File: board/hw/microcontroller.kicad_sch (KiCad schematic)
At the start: 2 parts, among them U1 RP2040, Y1 Crystal

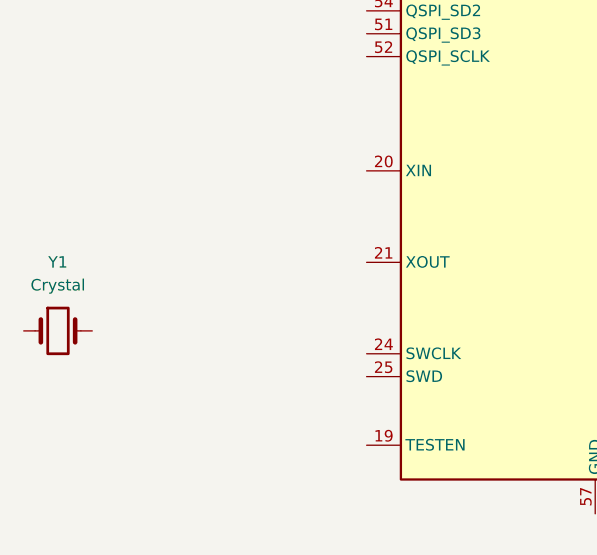
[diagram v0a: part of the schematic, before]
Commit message: added cristal oscillator with capacitors, and 3.3V LDO voltage regulator
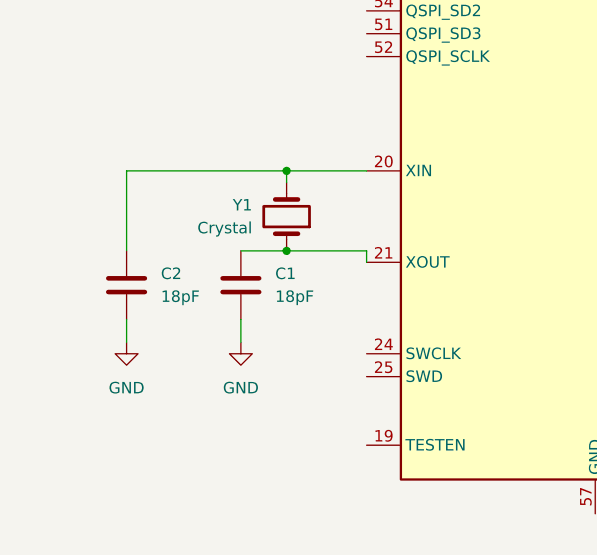
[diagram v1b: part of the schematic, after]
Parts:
- added C1, C2: 18pF, Capacitor_SMD:C_0603_1608Metric, symbol Device:C
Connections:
- net at U1.20 (XIN): now also Y1.2, C2.1
- net at U1.21 (XOUT): now also Y1.1, C1.1
- new net GND: C1.2, C2.2
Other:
- moved on the sheet: Y1
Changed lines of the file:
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@@
 (kicad_sch (version 20230121) (generator eeschema)
   (paper "A4")
+  (junction (at 114.3 101.6) (diameter 0) (color 0 0 0 0)
+  )
+  (junction (at 114.3 110.49) (diameter 0) (color 0 0 0 0)
+  )
+  (wire (pts (xy 96.52 118.11) (xy 96.52 120.65))
+    (stroke (width 0) (type default))
+  )
+  (wire (pts (xy 114.3 101.6) (xy 114.3 102.87))
+    (stroke (width 0) (type default))
+  )
+  (wire (pts (xy 109.22 110.49) (xy 114.3 110.49))
+    (stroke (width 0) (type default))
+  )
+  (wire (pts (xy 123.19 110.49) (xy 123.19 111.76))
+    (stroke (width 0) (type default))
+  )
+  (wire (pts (xy 96.52 101.6) (xy 114.3 101.6))
+    (stroke (width 0) (type default))
+  )
+  (wire (pts (xy 123.19 101.6) (xy 114.3 101.6))
+    (stroke (width 0) (type default))
+  )
+  (wire (pts (xy 109.22 118.11) (xy 109.22 120.65))
+    (stroke (width 0) (type default))
+  )
+  (wire (pts (xy 96.52 110.49) (xy 96.52 101.6))
+    (stroke (width 0) (type default))
+  )
+  (wire (pts (xy 114.3 110.49) (xy 123.19 110.49))
+    (stroke (width 0) (type default))
+  )
   (symbol (lib_id "MCU_RaspberryPi:RP2040") (at 148.59 93.98 0) (unit 1)
     (in_bom yes) (on_board yes) (dnp no) (fields_autoplaced)
@@
     )
   )
-  (symbol (lib_id "Device:Crystal") (at 88.9 119.38 0) (unit 1)
-    (in_bom yes) (on_board yes) (dnp no) (fields_autoplaced)
-    (property "Reference" "Y1" (at 88.9 111.76 0)
+  (symbol (lib_id "Device:Crystal") (at 114.3 106.68 270) (mirror x) (unit 1)
+    (in_bom yes) (on_board yes) (dnp no)
+    (property "Reference" "Y1" (at 110.49 105.41 90)
+      (effects (font (size 1.27 1.27)) (justify right))
+    )
+    (property "Value" "Crystal" (at 110.49 107.95 90)
+      (effects (font (size 1.27 1.27)) (justify right))
+    )
+    (property "Footprint" "Crystal:Crystal_SMD_SeikoEpson_MA505-2Pin_12.7x5.1mm" (at 114.3 106.68 0)
+      (effects (font (size 1.27 1.27)) hide)
+    )
+    (property "Datasheet" "~" (at 114.3 106.68 0)
+      (effects (font (size 1.27 1.27)) hide)
+    )
+    (pin "2")
+    (pin "1")
+    (instances
+      (project "yals"
+        (path "/920838ab-42d6-4f6a-a4ed-bf4606dd42d5/8ac632fc-8d3b-4983-8745-f2671c397aa7"
+          (reference "Y1") (unit 1)
+        )
+      )
+    )
+  )
+  (symbol (lib_id "Device:C") (at 96.52 114.3 0) (unit 1)
+    (in_bom yes) (on_board yes) (dnp no) (fields_autoplaced)
+    (property "Reference" "C2" (at 100.33 113.03 0)
+      (effects (font (size 1.27 1.27)) (justify left))
+    )
+    (property "Value" "18pF" (at 100.33 115.57 0)
+      (effects (font (size 1.27 1.27)) (justify left))
+    )
+    (property "Footprint" "Capacitor_SMD:C_0603_1608Metric" (at 97.4852 118.11 0)
+      (effects (font (size 1.27 1.27)) hide)
+    )
+    (property "Datasheet" "~" (at 96.52 114.3 0)
+      (effects (font (size 1.27 1.27)) hide)
+    )
+    (pin "1")
+    (pin "2")
+    (instances
+      (project "yals"
+        (path "/920838ab-42d6-4f6a-a4ed-bf4606dd42d5/8ac632fc-8d3b-4983-8745-f2671c397aa7"
+          (reference "C2") (unit 1)
+        )
+      )
+    )
+  )
+  (symbol (lib_id "power:GND") (at 109.22 120.65 0) (unit 1)
+    (in_bom yes) (on_board yes) (dnp no) (fields_autoplaced)
+    (property "Reference" "#PWR04" (at 109.22 127 0)
+      (effects (font (size 1.27 1.27)) hide)
+    )
+    (property "Value" "GND" (at 109.22 125.73 0)
       (effects (font (size 1.27 1.27)))
     )
-    (property "Value" "Crystal" (at 88.9 114.3 0)
+    (property "Footprint" "" (at 109.22 120.65 0)
+      (effects (font (size 1.27 1.27)) hide)
+    )
+    (property "Datasheet" "" (at 109.22 120.65 0)
+      (effects (font (size 1.27 1.27)) hide)
+    )
+    (pin "1")
+    (instances
+      (project "yals"
+        (path "/920838ab-42d6-4f6a-a4ed-bf4606dd42d5/8ac632fc-8d3b-4983-8745-f2671c397aa7"
+          (reference "#PWR04") (unit 1)
+        )
+      )
+    )
+  )
+  (symbol (lib_id "Device:C") (at 109.22 114.3 0) (unit 1)
+    (in_bom yes) (on_board yes) (dnp no) (fields_autoplaced)
+    (property "Reference" "C1" (at 113.03 113.03 0)
+      (effects (font (size 1.27 1.27)) (justify left))
+    )
+    (property "Value" "18pF" (at 113.03 115.57 0)
+      (effects (font (size 1.27 1.27)) (justify left))
+    )
+    (property "Footprint" "Capacitor_SMD:C_0603_1608Metric" (at 110.1852 118.11 0)
+      (effects (font (size 1.27 1.27)) hide)
+    )
+    (property "Datasheet" "~" (at 109.22 114.3 0)
+      (effects (font (size 1.27 1.27)) hide)
+    )
+    (pin "1")
+    (pin "2")
+    (instances
+      (project "yals"
+        (path "/920838ab-42d6-4f6a-a4ed-bf4606dd42d5/8ac632fc-8d3b-4983-8745-f2671c397aa7"
+          (reference "C1") (unit 1)
+        )
+      )
+    )
+  )
+  (symbol (lib_id "power:GND") (at 96.52 120.65 0) (unit 1)
+    (in_bom yes) (on_board yes) (dnp no) (fields_autoplaced)
+    (property "Reference" "#PWR05" (at 96.52 127 0)
+      (effects (font (size 1.27 1.27)) hide)
+    )
+    (property "Value" "GND" (at 96.52 125.73 0)
       (effects (font (size 1.27 1.27)))
     )
-    (property "Footprint" "Crystal:Crystal_SMD_SeikoEpson_MA505-2Pin_12.7x5.1mm" (at 88.9 119.38 0)
-      (effects (font (size 1.27 1.27)) hide)
-    )
-    (property "Datasheet" "~" (at 88.9 119.38 0)
-      (effects (font (size 1.27 1.27)) hide)
-    )
-    (pin "2")
-    (pin "1")
-    (instances
-      (project "yals"
-        (path "/920838ab-42d6-4f6a-a4ed-bf4606dd42d5/8ac632fc-8d3b-4983-8745-f2671c397aa7"
-          (reference "Y1") (unit 1)
-        )
-      )
+    (property "Footprint" "" (at 96.52 120.65 0)
+      (effects (font (size 1.27 1.27)) hide)
+    )
+    (property "Datasheet" "" (at 96.52 120.65 0)
+      (effects (font (size 1.27 1.27)) hide)
+    )
+    (pin "1")
+    (instances
+      (project "yals"
+        (path "/920838ab-42d6-4f6a-a4ed-bf4606dd42d5/8ac632fc-8d3b-4983-8745-f2671c397aa7"
+          (reference "#PWR05") (unit 1)
+        )
+      )

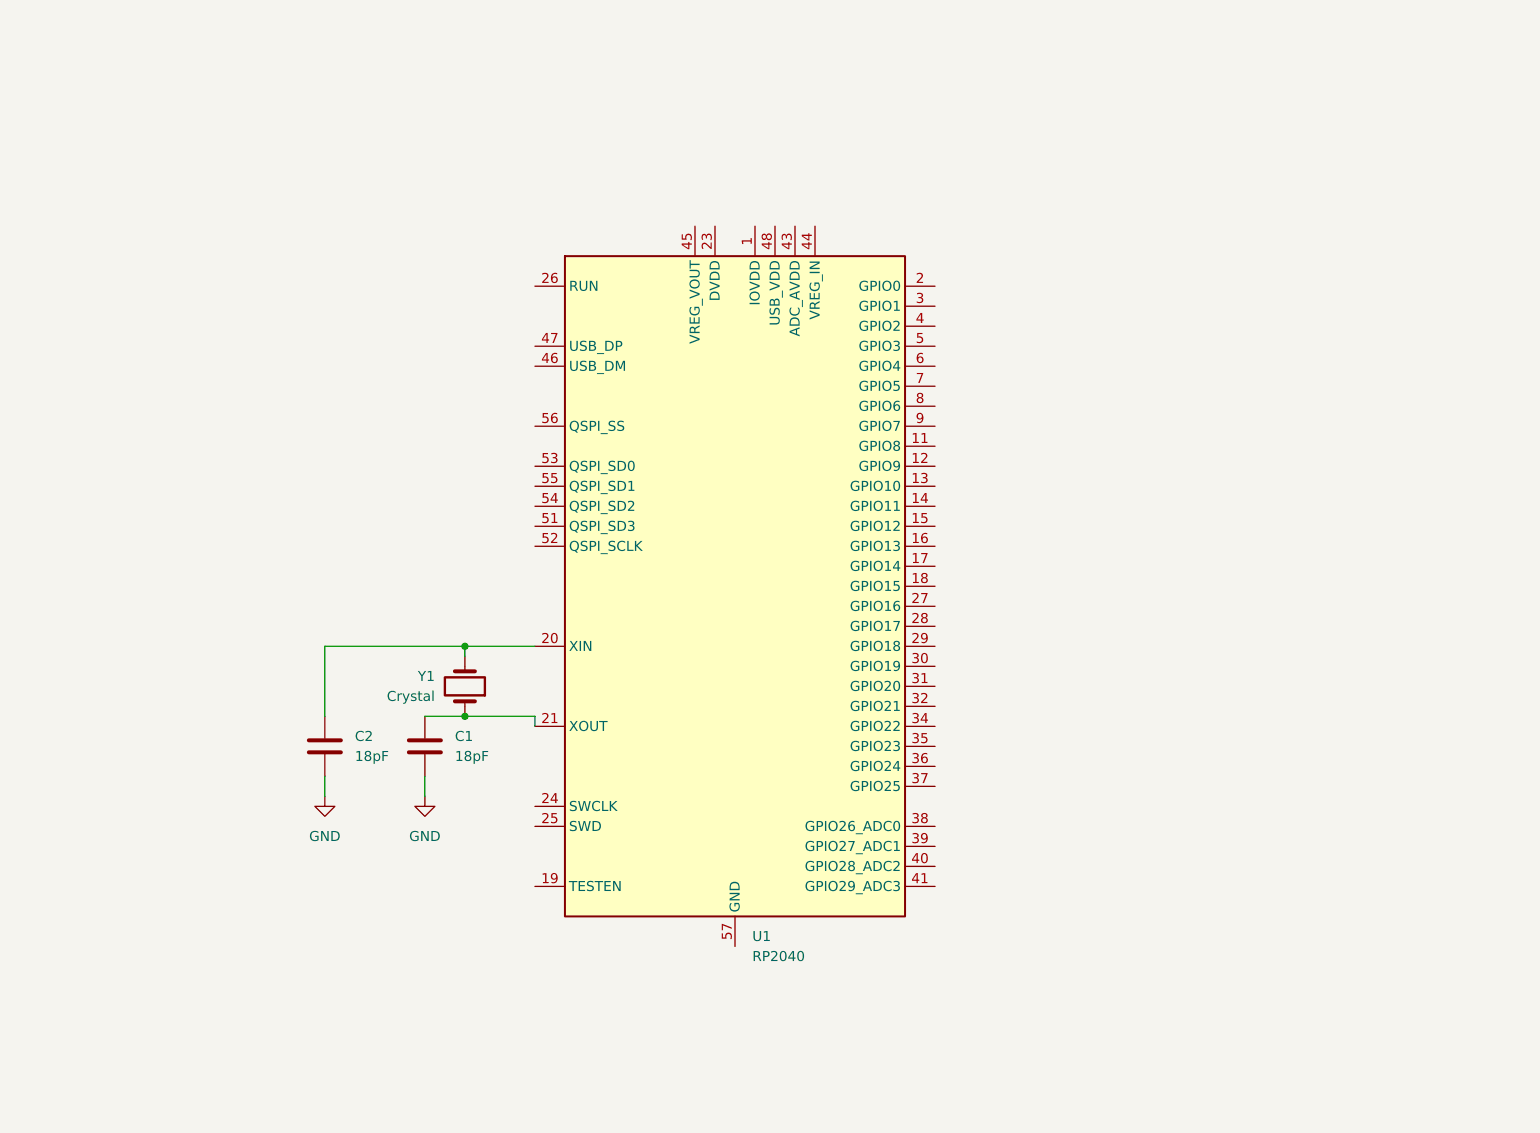
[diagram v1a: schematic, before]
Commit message: rp2040 and its connections are nearly done (still missing power-measuring capabilities)
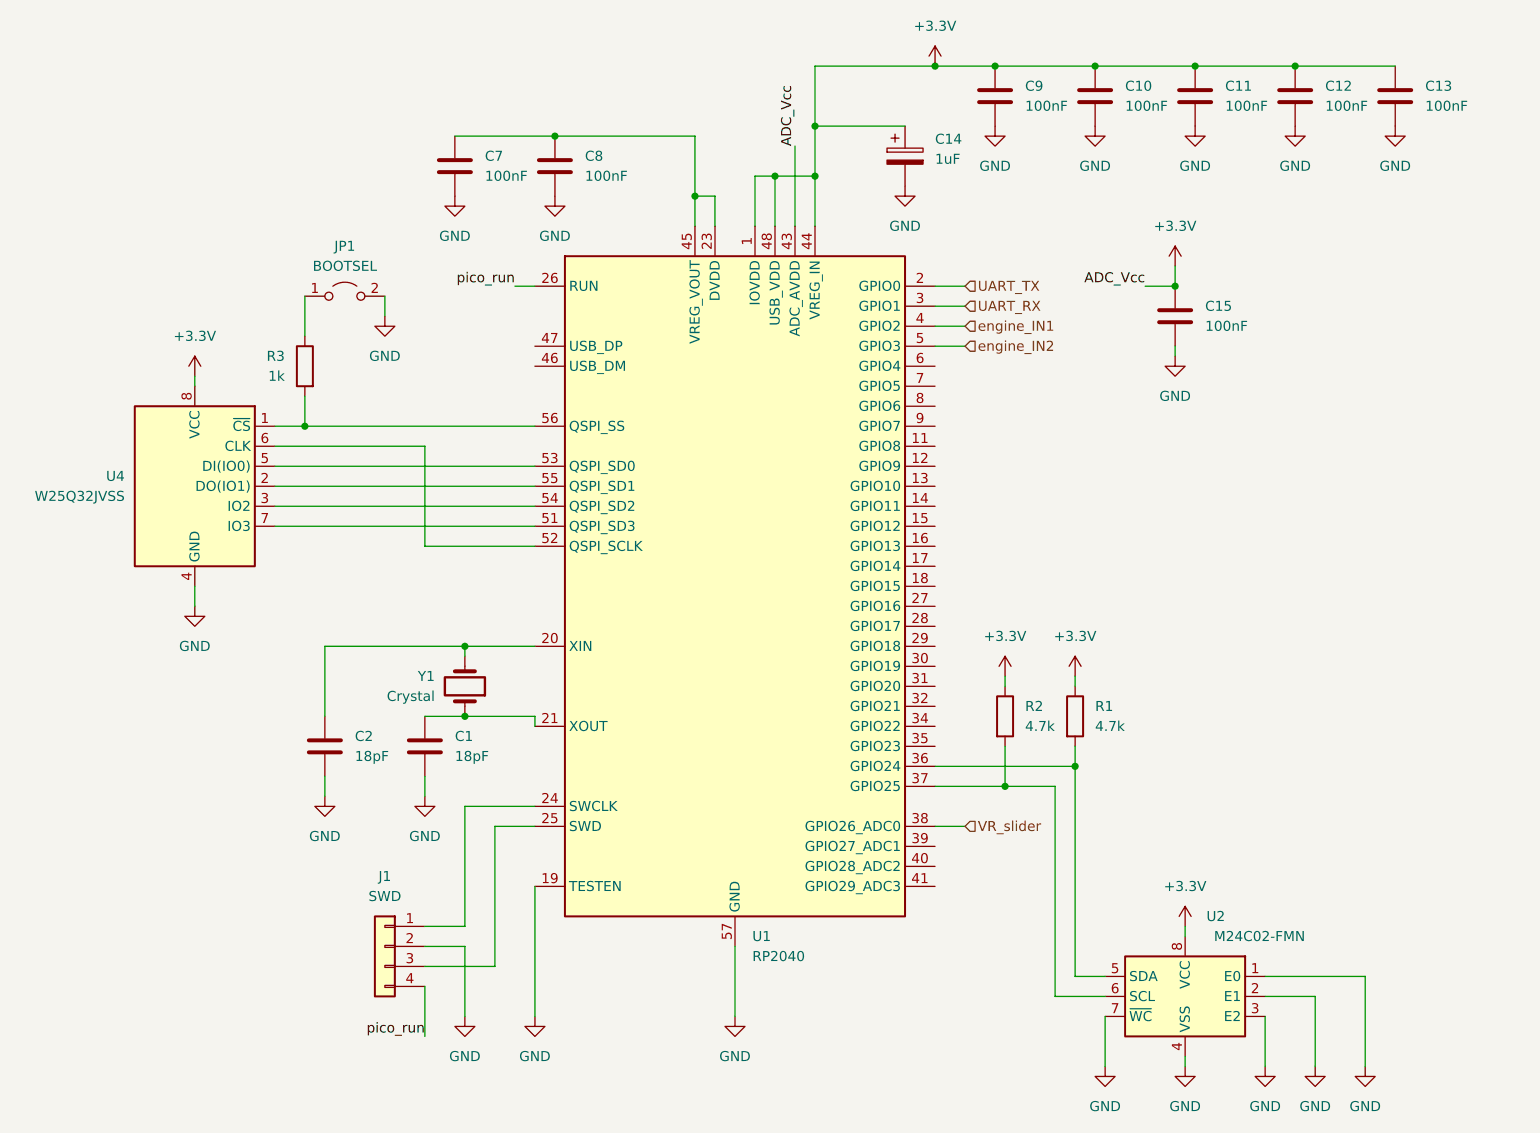
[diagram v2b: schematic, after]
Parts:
- added C10, C11, C12, C13, C15, C7, C8, C9: 100nF, Capacitor_SMD:C_1206_3216Metric, symbol Device:C
- added C14: 1uF, Capacitor_SMD:CP_Elec_5x4.5, symbol Device:C_Polarized
- added J1: SWD, Connector_PinHeader_2.54mm:PinHeader_1x04_P2.54mm_Vertical, symbol Connector_Generic:Conn_01x04
- added JP1: BOOTSEL, Connector_PinHeader_2.54mm:PinHeader_1x02_P2.54mm_Vertical, symbol Jumper:Jumper_2_Open
- added R1, R2: 4.7k, Resistor_SMD:R_0603_1608Metric, symbol Device:R
- added R3: 1k, Resistor_SMD:R_0603_1608Metric, symbol Device:R
- added U2: M24C02-FMN, Package_SO:SOIC-8_3.9x4.9mm_P1.27mm, symbol Memory_EEPROM:M24C02-FMN
- added U4: W25Q32JVSS, Package_SO:SOIC-8_5.23x5.23mm_P1.27mm, symbol Memory_Flash:W25Q32JVSS
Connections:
- net GND: now also U1.19 (TESTEN), U1.57 (GND), C10.2, C11.2, C12.2, C13.2, C14.2, C15.2, C7.2, C8.2, C9.2, J1.2 (Pin_2), JP1.2 (B), U2.1 (E0), U2.2 (E1), U2.3 (E2), U2.4 (VSS), U2.7 (~{WC}), U4.4 (GND)
- net +3.3V: now reaches U1.1 (IOVDD), U1.10 (IOVDD), U1.22 (IOVDD), U1.33 (IOVDD), U1.42 (IOVDD), U1.49 (IOVDD)
- net +3.3V: now also U1.43 (ADC_AVDD), U1.44 (VREG_IN), U1.48 (USB_VDD), C10.1, C11.1, C12.1, C13.1, C14.1, C15.1, C9.1, R1.1, R2.1, U2.8 (VCC), U4.8 (VCC)
- net UART_TX: now reaches U1.2 (GPIO0)
- net at U1.23 (DVDD), U1.50 (DVDD): now also U1.45 (VREG_VOUT), C7.1, C8.1
- net at U1.24 (SWCLK): now also J1.1 (Pin_1)
- net at U1.25 (SWD): now also J1.3 (Pin_3)
- net pico_run: now reaches U1.26 (RUN)
- net pico_run: now also J1.4 (Pin_4)
- net UART_RX: now reaches U1.3 (GPIO1)
- net at U1.36 (GPIO24): now also R1.2, U2.5 (SDA)
- net at U1.37 (GPIO25): now also R2.2, U2.6 (SCL)
- net VR_slider: now reaches U1.38 (GPIO26_ADC0)
- net engine_IN1: now reaches U1.4 (GPIO2)
- net engine_IN2: now reaches U1.5 (GPIO3)
- net at U1.51 (QSPI_SD3): now also U4.7 (IO3)
- net at U1.52 (QSPI_SCLK): now also U4.6 (CLK)
- net at U1.53 (QSPI_SD0): now also U4.5 (DI(IO0))
- net at U1.54 (QSPI_SD2): now also U4.3 (IO2)
- net at U1.55 (QSPI_SD1): now also U4.2 (DO(IO1))
- net at U1.56 (QSPI_SS): now also R3.2, U4.1 (~{CS})
- new net: JP1.1 (A), R3.1

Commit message: * moved potentiometer to engine's sheet * added engine's Vcc feedback
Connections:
- net eng_Vcc_feedback: now reaches U1.39 (GPIO27_ADC1)
- net VR_slider renamed eng_pos_feedback
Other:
- moved on the sheet: U2

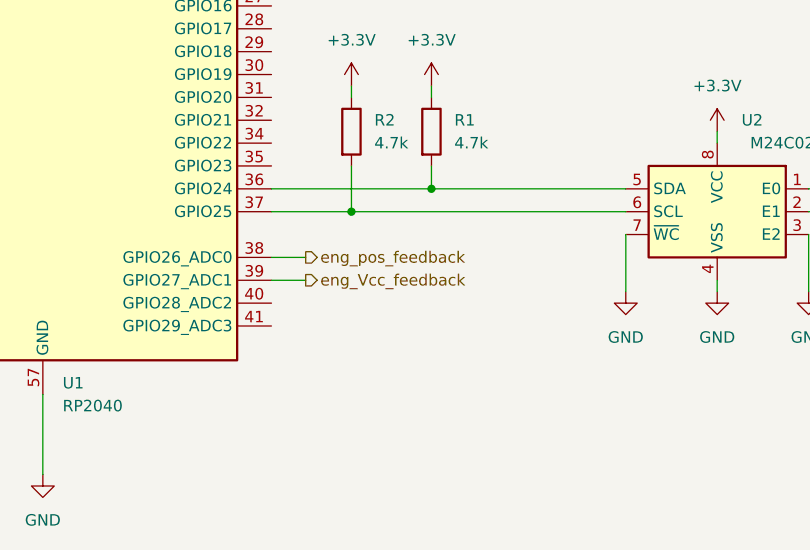
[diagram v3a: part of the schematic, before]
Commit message: fixed feedback pins directions
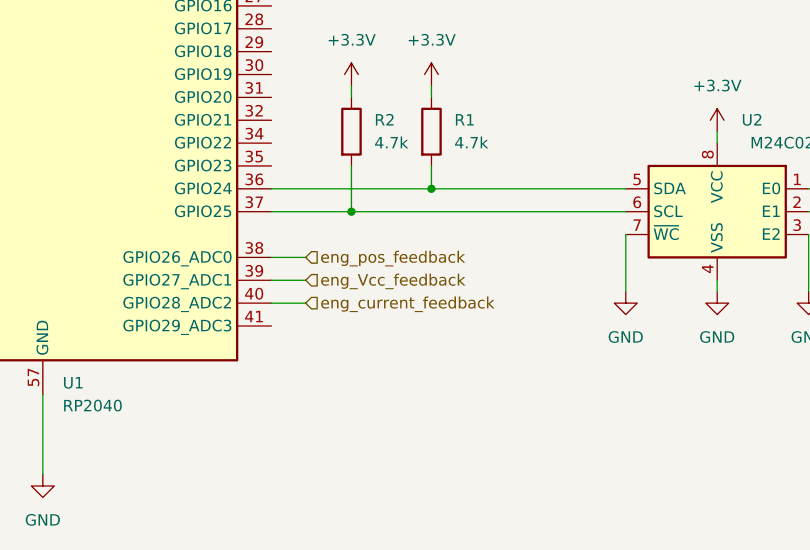
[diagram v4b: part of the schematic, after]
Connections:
- net eng_current_feedback: now reaches U1.40 (GPIO28_ADC2)
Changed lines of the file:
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@@
+    (stroke (width 0) (type default))
+  )
+  (wire (pts (xy 177.8 129.54) (xy 173.99 129.54))
     (stroke (width 0) (type default))
   )
@@
     (effects (font (size 1.27 1.27)) (justify left bottom))
   )
-  (hierarchical_label "eng_Vcc_feedback" (shape output) (at 177.8 127 0) (fields_autoplaced)
+  (hierarchical_label "eng_Vcc_feedback" (shape input) (at 177.8 127 0) (fields_autoplaced)
     (effects (font (size 1.27 1.27)) (justify left))
   )
@@
     (effects (font (size 1.27 1.27)) (justify left))
   )
-  (hierarchical_label "eng_pos_feedback" (shape output) (at 177.8 124.46 0) (fields_autoplaced)
-    (effects (font (size 1.27 1.27)) (justify left))
-  )
+  (hierarchical_label "eng_current_feedback" (shape input) (at 177.8 129.54 0) (fields_autoplaced)
+    (effects (font (size 1.27 1.27)) (justify left))
+  )
+  (hierarchical_label "eng_pos_feedback" (shape input) (at 177.8 124.46 0) (fields_autoplaced)
+    (effects (font (size 1.27 1.27)) (justify left))
+  )
